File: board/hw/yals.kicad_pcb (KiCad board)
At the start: 2 copper layers, 1 part

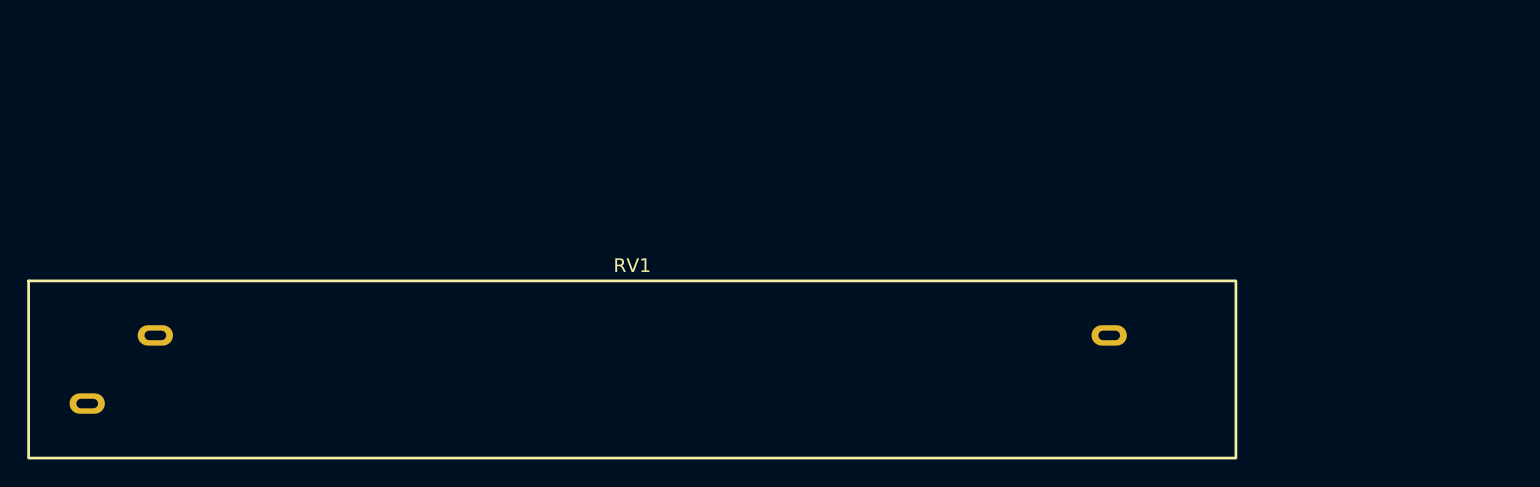
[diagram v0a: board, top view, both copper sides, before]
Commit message: added 2 sub-sheets for µC and power
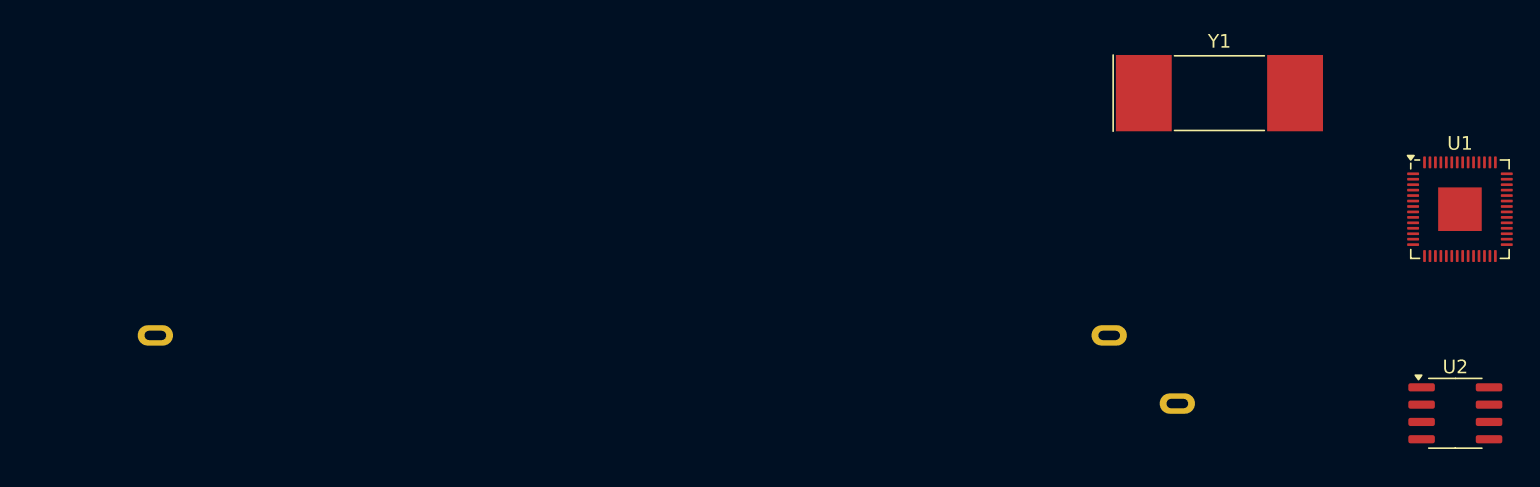
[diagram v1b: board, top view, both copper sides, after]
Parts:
- added U1: RP2040, Package_DFN_QFN:QFN-56-1EP_7x7mm_P0.4mm_EP3.2x3.2mm, F.Cu at (168.0, 66.9)
- added U2: LM78L05_SO8, Package_SO:SOIC-8_3.9x4.9mm_P1.27mm, F.Cu at (167.6, 81.9)
- added Y1: Crystal, Crystal:Crystal_SMD_SeikoEpson_MA505-2Pin_12.7x5.1mm, F.Cu at (150.3, 58.4)
- RV1: moved to B.Cu
- turned RV1 to 180 degrees

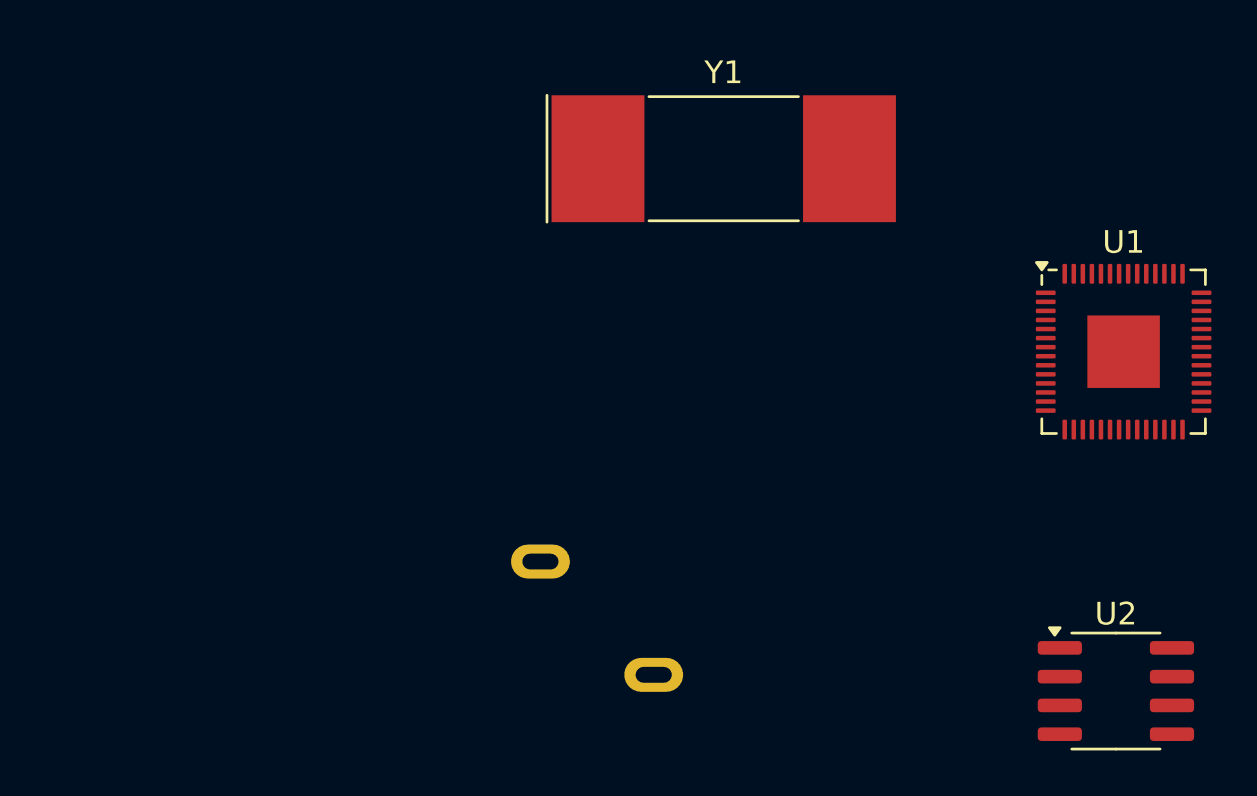
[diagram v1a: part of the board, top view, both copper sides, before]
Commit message: added cristal oscillator with capacitors, and 3.3V LDO voltage regulator
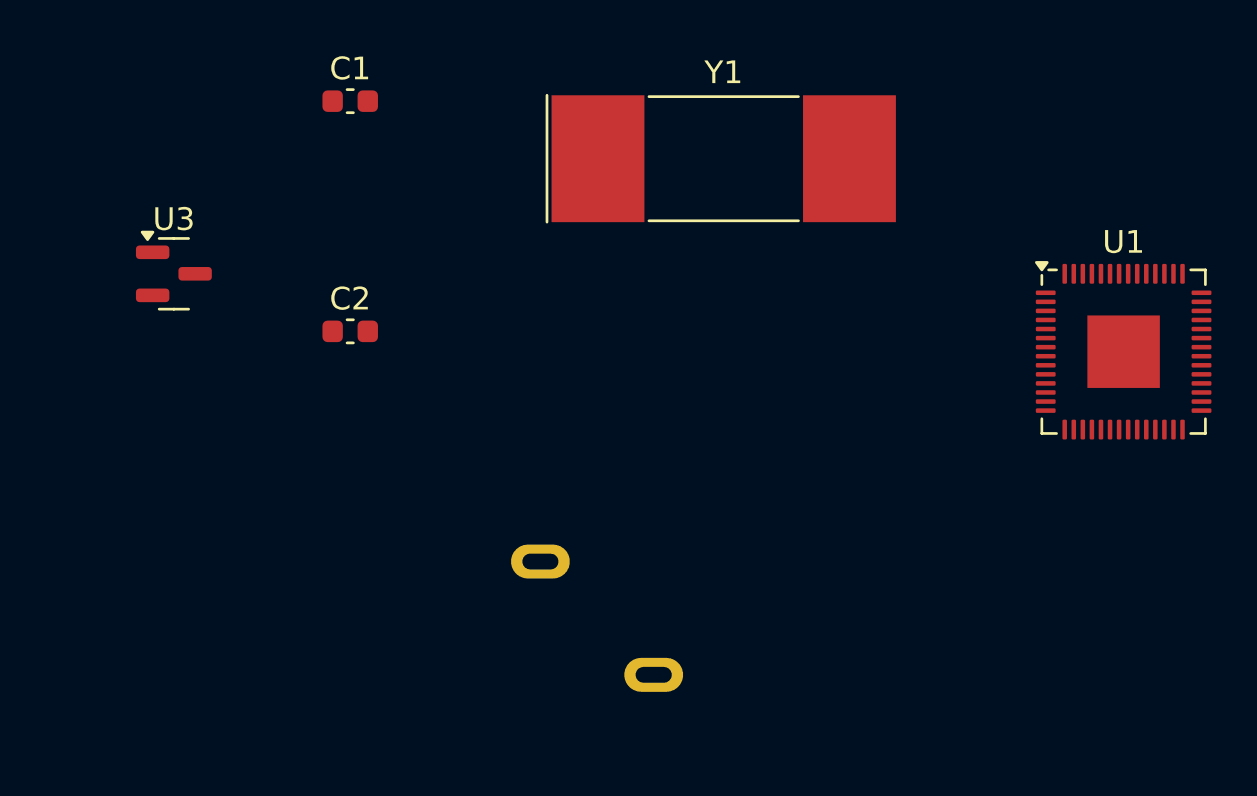
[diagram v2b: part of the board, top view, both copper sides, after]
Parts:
- removed U2: LM78L05_SO8, Package_SO:SOIC-8_3.9x4.9mm_P1.27mm
- added C1: 18pF, Capacitor_SMD:C_0603_1608Metric, F.Cu at (133.8, 55.9)
- added C2: 18pF, Capacitor_SMD:C_0603_1608Metric, F.Cu at (133.8, 66.0)
- added U3: MCP1703Ax-330xxTT, Package_TO_SOT_SMD:SOT-23, F.Cu at (126.1, 63.5)
- RV1: value R_Potentiometer -> CDE23N-60-B50K
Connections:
- RV1 pad 1: unconnected-(RV1-Pad1) -> +3.3V
- RV1 pad 3: unconnected-(RV1-Pad3) -> GND
- U1 pad 20: unconnected-(U1-XIN-Pad20) -> Net-(U1-XIN)
- U1 pad 21: unconnected-(U1-XOUT-Pad21) -> Net-(U1-XOUT)
- Y1 pad 1: unconnected-(Y1-Pad1) -> Net-(U1-XOUT)
- Y1 pad 2: unconnected-(Y1-Pad2) -> Net-(U1-XIN)

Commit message: power block is almost ready
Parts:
- added C3: 100nF, Capacitor_SMD:C_1206_3216Metric, F.Cu at (123.0, 43.2)
- added C4: 4.7uF, Capacitor_SMD:CP_Elec_5x4.5, F.Cu at (114.6, 37.1)
- added C5: 10uF, Capacitor_SMD:CP_Elec_5x4.5, F.Cu at (114.6, 44.0)
- added C6: 100nF, Capacitor_SMD:C_1206_3216Metric, F.Cu at (114.6, 50.8)
- added D1: TS418C, Diode_SMD:D_0603_1608Metric, F.Cu at (123.7, 35.6)
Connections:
- U3 pad 3: +12V -> Net-(D1-K)

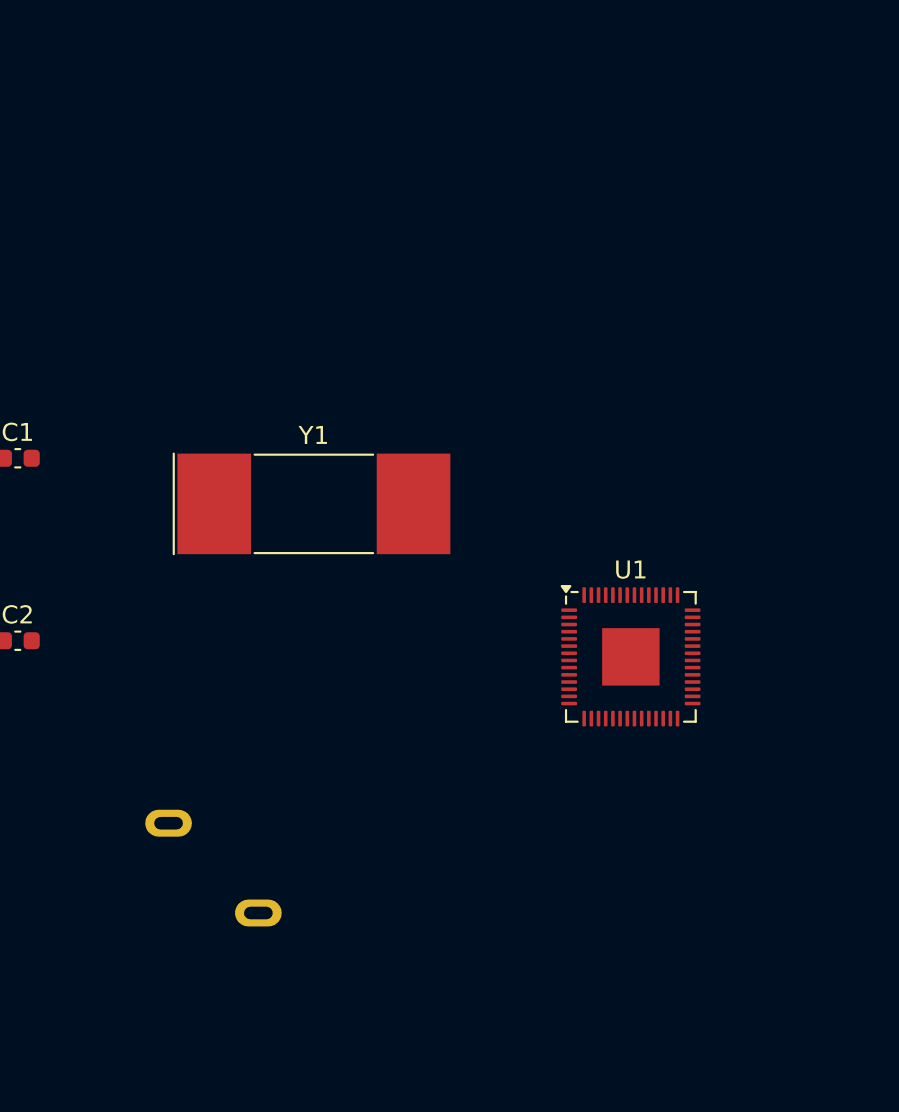
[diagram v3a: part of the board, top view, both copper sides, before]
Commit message: rp2040 and its connections are nearly done (still missing power-measuring capabilities)
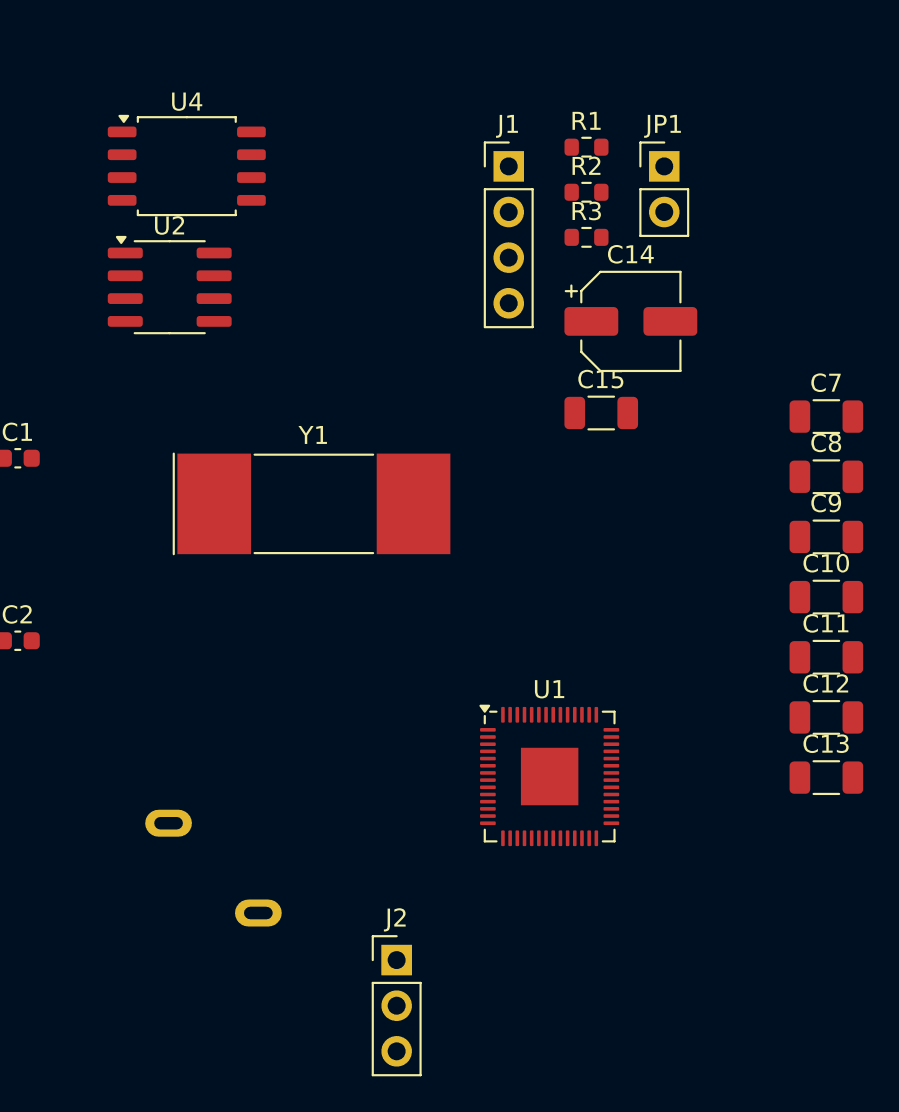
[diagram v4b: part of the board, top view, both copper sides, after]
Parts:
- added C10: 100nF, Capacitor_SMD:C_1206_3216Metric, F.Cu at (178.9, 63.6)
- added C11: 100nF, Capacitor_SMD:C_1206_3216Metric, F.Cu at (178.9, 67.0)
- added C12: 100nF, Capacitor_SMD:C_1206_3216Metric, F.Cu at (178.9, 70.3)
- added C13: 100nF, Capacitor_SMD:C_1206_3216Metric, F.Cu at (178.9, 73.7)
- added C14: 1uF, Capacitor_SMD:CP_Elec_5x4.5, F.Cu at (168.0, 48.3)
- added C15: 100nF, Capacitor_SMD:C_1206_3216Metric, F.Cu at (166.3, 53.4)
- added C7: 100nF, Capacitor_SMD:C_1206_3216Metric, F.Cu at (178.9, 53.6)
- added C8: 100nF, Capacitor_SMD:C_1206_3216Metric, F.Cu at (178.9, 56.9)
- added C9: 100nF, Capacitor_SMD:C_1206_3216Metric, F.Cu at (178.9, 60.3)
- added J1: SWD, Connector_PinHeader_2.54mm:PinHeader_1x04_P2.54mm_Vertical, F.Cu at (161.2, 39.6)
- added J2: UART, Connector_PinHeader_2.54mm:PinHeader_1x03_P2.54mm_Vertical, F.Cu at (154.9, 83.8)
- added JP1: BOOTSEL, Connector_PinHeader_2.54mm:PinHeader_1x02_P2.54mm_Vertical, F.Cu at (169.8, 39.6)
- added R1: 4.7k, Resistor_SMD:R_0603_1608Metric, F.Cu at (165.5, 38.6)
- added R2: 4.7k, Resistor_SMD:R_0603_1608Metric, F.Cu at (165.5, 41.1)
- added R3: 1k, Resistor_SMD:R_0603_1608Metric, F.Cu at (165.5, 43.6)
- added U2: M24C02-FMN, Package_SO:SOIC-8_3.9x4.9mm_P1.27mm, F.Cu at (142.3, 46.4)
- added U4: W25Q32JVSS, Package_SO:SOIC-8_5.23x5.23mm_P1.27mm, F.Cu at (143.3, 39.6)
- moved U1 8.05 mm to (163.5, 73.6)
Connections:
- RV1 pad 2: unconnected-(RV1-Pad2) -> /microcontroller/VR_slider
- U1 pad 1: Net-(U1-IOVDD-Pad1) -> +3.3V
- U1 pad 10: Net-(U1-IOVDD-Pad1) -> +3.3V
- U1 pad 19: unconnected-(U1-TESTEN-Pad19) -> GND
- U1 pad 2: unconnected-(U1-GPIO0-Pad2) -> /microcontroller/UART_TX
- U1 pad 22: Net-(U1-IOVDD-Pad1) -> +3.3V
- U1 pad 23: Net-(U1-DVDD-Pad23) -> Net-(U1-VREG_VOUT)
- U1 pad 24: unconnected-(U1-SWCLK-Pad24) -> Net-(J1-Pin_1)
- U1 pad 25: unconnected-(U1-SWD-Pad25) -> Net-(J1-Pin_3)
- U1 pad 26: unconnected-(U1-RUN-Pad26) -> /microcontroller/pico_run
- U1 pad 3: unconnected-(U1-GPIO1-Pad3) -> /microcontroller/UART_RX
- U1 pad 33: Net-(U1-IOVDD-Pad1) -> +3.3V
- U1 pad 36: unconnected-(U1-GPIO24-Pad36) -> Net-(U1-GPIO24)
- U1 pad 37: unconnected-(U1-GPIO25-Pad37) -> Net-(U1-GPIO25)
- U1 pad 38: unconnected-(U1-GPIO26_ADC0-Pad38) -> /microcontroller/VR_slider
- U1 pad 4: unconnected-(U1-GPIO2-Pad4) -> /microcontroller/engine_IN1
- U1 pad 42: Net-(U1-IOVDD-Pad1) -> +3.3V
- U1 pad 43: unconnected-(U1-ADC_AVDD-Pad43) -> +3.3V
- U1 pad 44: unconnected-(U1-VREG_IN-Pad44) -> +3.3V
- U1 pad 45: unconnected-(U1-VREG_VOUT-Pad45) -> Net-(U1-VREG_VOUT)
- U1 pad 48: unconnected-(U1-USB_VDD-Pad48) -> +3.3V
- U1 pad 49: Net-(U1-IOVDD-Pad1) -> +3.3V
- U1 pad 5: unconnected-(U1-GPIO3-Pad5) -> /microcontroller/engine_IN2
- U1 pad 50: Net-(U1-DVDD-Pad23) -> Net-(U1-VREG_VOUT)
- U1 pad 51: unconnected-(U1-QSPI_SD3-Pad51) -> Net-(U1-QSPI_SD3)
- U1 pad 52: unconnected-(U1-QSPI_SCLK-Pad52) -> Net-(U1-QSPI_SCLK)
- U1 pad 53: unconnected-(U1-QSPI_SD0-Pad53) -> Net-(U1-QSPI_SD0)
- U1 pad 54: unconnected-(U1-QSPI_SD2-Pad54) -> Net-(U1-QSPI_SD2)
- U1 pad 55: unconnected-(U1-QSPI_SD1-Pad55) -> Net-(U1-QSPI_SD1)
- U1 pad 56: unconnected-(U1-QSPI_SS-Pad56) -> Net-(U1-QSPI_SS)
- U1 pad 57: unconnected-(U1-GND-Pad57) -> GND

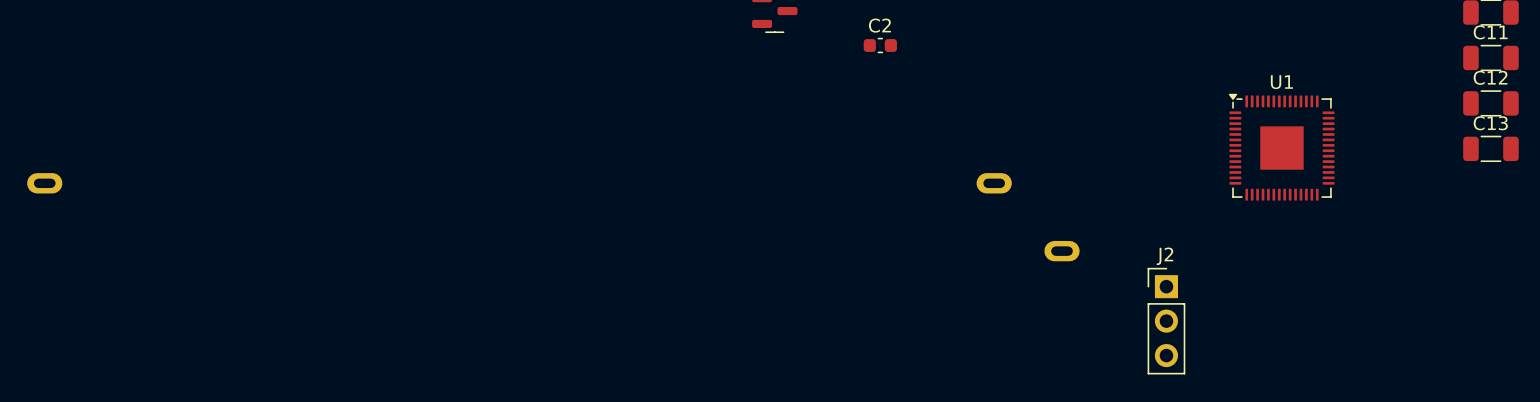
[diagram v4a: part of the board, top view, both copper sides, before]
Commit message: * moved potentiometer to engine's sheet * added engine's Vcc feedback
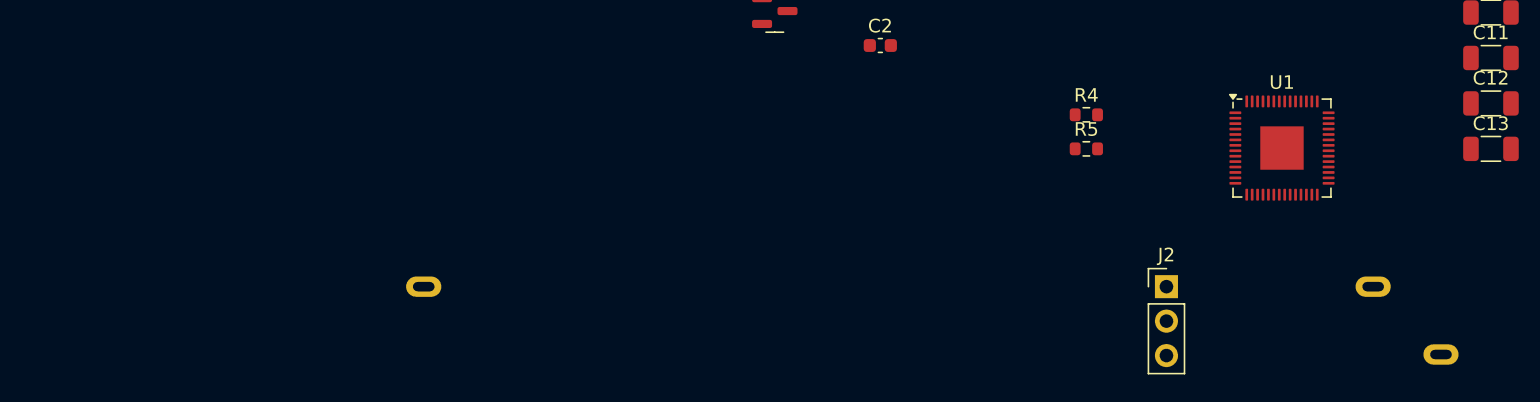
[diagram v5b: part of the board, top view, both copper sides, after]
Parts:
- added R4: 100k, Resistor_SMD:R_0603_1608Metric, F.Cu at (149.0, 71.2)
- added R5: 100k, Resistor_SMD:R_0603_1608Metric, F.Cu at (149.0, 73.7)
- moved RV1 29.0 mm to (135.2, 86.3)
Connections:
- net /microcontroller/VR_slider renamed /engine ctrl/eng_pos_feedback
- U1 pad 39: unconnected-(U1-GPIO27_ADC1-Pad39) -> /engine ctrl/eng_Vcc_feedback
